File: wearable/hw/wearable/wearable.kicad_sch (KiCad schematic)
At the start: 101 parts, among them J2 Conn_02x05_Odd_Even, J3 USB-C Connector, SW1 SW_Toggle, U1 ADS1299IPAG, U2 TPD1E05U06DYA, U3 BNO080, U4 nPM1300-QEXX, U5 LT3042xMSE, U6 TPS61040DBV, U7 BL54L15-453-000xxx, Y1 32.768kHz, Y2 32.768kHz

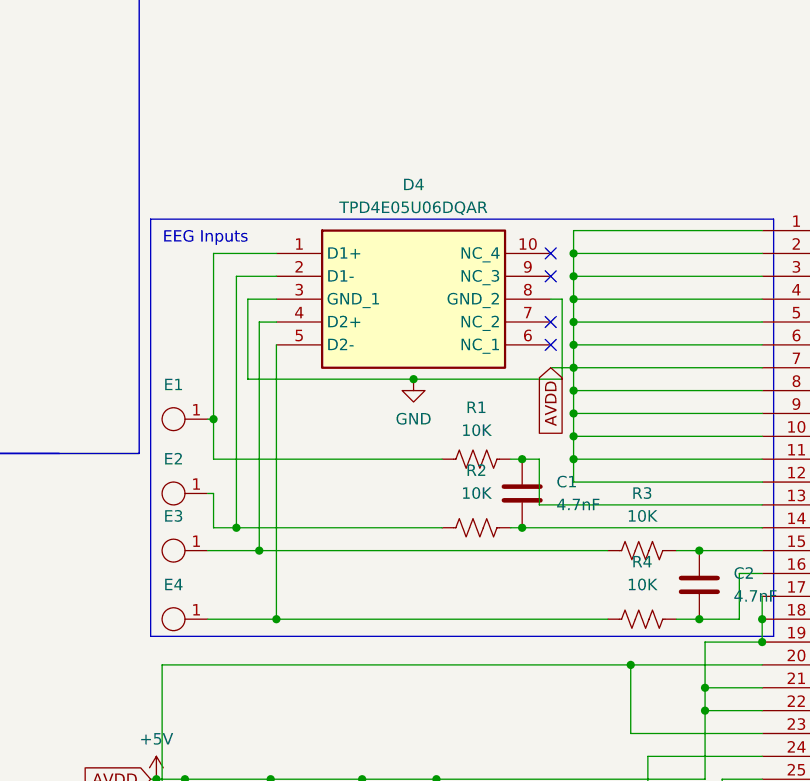
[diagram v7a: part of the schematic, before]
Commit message: Printout documents, reworked analog inputs
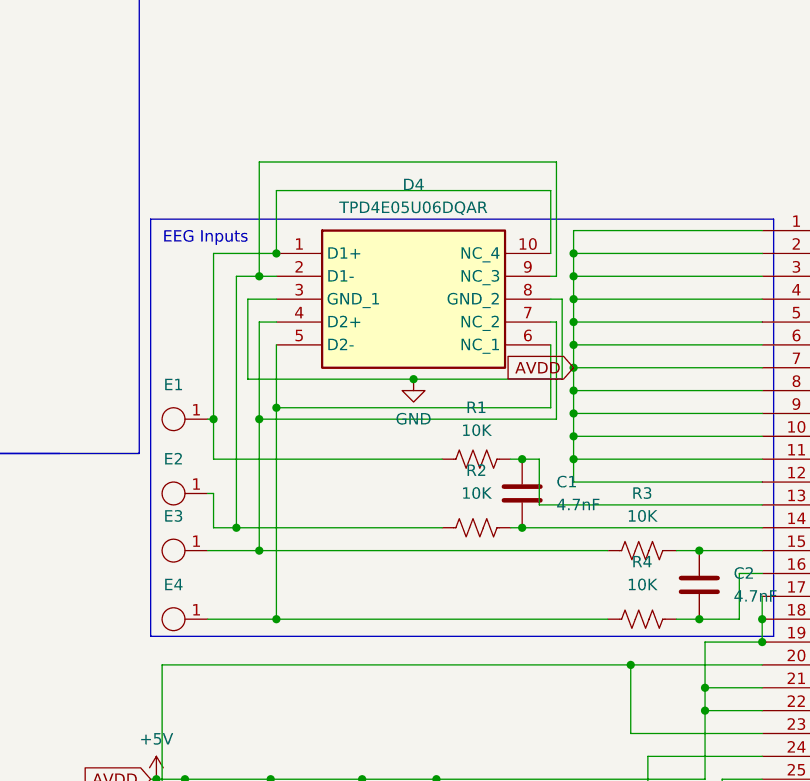
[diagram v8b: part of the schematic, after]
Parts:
- D4: footprint DQA(R-PUSON-N10) -> PCM_Package_SON_AKL:USON-10_2.5x1.0mm_P0.5mm
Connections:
- net at D4.4 (D2+), E3.1, R3.2: now also D4.7 (NC_2)
- net at D4.2 (D1-), E2.1, R2.2: now also D4.9 (NC_3)
- net at D4.1 (D1+), E1.1, R1.2: now also D4.10 (NC_4)
- net at D4.5 (D2-), E4.1, R4.2: now also D4.6 (NC_1)
- no-connect marks 34 -> 30
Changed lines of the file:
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@@
 	)
 	(junction
+		(at 215.265 168.275)
+		(diameter 0)
+		(color 0 0 0 0)
+	)
+	(junction
 		(at 168.275 195.58)
 		(diameter 0)
@@
 	)
 	(junction
+		(at 217.17 182.88)
+		(diameter 0)
+		(color 0 0 0 0)
+	)
+	(junction
 		(at 34.925 288.925)
 		(diameter 0)
@@
 	)
 	(junction
+		(at 217.17 165.735)
+		(diameter 0)
+		(color 0 0 0 0)
+	)
+	(junction
 		(at 10.795 288.925)
 		(diameter 0)
@@
 	)
 	(junction
+		(at 215.265 184.15)
+		(diameter 0)
+		(color 0 0 0 0)
+	)
+	(junction
 		(at 361.315 186.055)
 		(diameter 0)
@@
 	)
 	(no_connect
-		(at 247.65 175.895)
-	)
-	(no_connect
 		(at 299.085 81.915)
 	)
@@
 	)
 	(no_connect
-		(at 247.65 173.355)
-	)
-	(no_connect
 		(at 43.815 235.585)
 	)
@@
 	)
 	(no_connect
-		(at 247.65 168.275)
-	)
-	(no_connect
 		(at 118.745 32.385)
 	)
@@
 	)
 	(no_connect
-		(at 247.65 165.735)
-	)
-	(no_connect
 		(at 118.745 17.145)
 	)
@@
 	(wire
 		(pts
+			(xy 217.17 158.75) (xy 217.17 165.735)
+		)
+		(stroke
+			(width 0)
+			(type default)
+		)
+	)
+	(wire
+		(pts
 			(xy 79.375 203.835) (xy 81.915 203.835)
 		)
@@
 	(wire
 		(pts
-			(xy 217.17 175.895) (xy 217.17 206.375)
+			(xy 217.17 175.895) (xy 217.17 182.88)
 		)
 		(stroke
@@
 	(wire
 		(pts
+			(xy 215.265 168.275) (xy 212.725 168.275)
+		)
+		(stroke
+			(width 0)
+			(type default)
+		)
+	)
+	(wire
+		(pts
 			(xy 19.05 212.725) (xy 19.05 205.105)
 		)
@@
 	(wire
 		(pts
+			(xy 247.65 158.75) (xy 217.17 158.75)
+		)
+		(stroke
+			(width 0)
+			(type default)
+		)
+	)
+	(wire
+		(pts
 			(xy 25.4 282.575) (xy 25.4 288.925)
 		)
@@
 	(wire
 		(pts
-			(xy 247.65 178.435) (xy 250.19 178.435)
-		)
-		(stroke
-			(width 0)
-			(type default)
-		)
-	)
-	(wire
-		(pts
 			(xy 264.795 216.535) (xy 271.145 216.535)
 		)
@@
 	(wire
 		(pts
-			(xy 217.17 168.275) (xy 212.725 168.275)
+			(xy 217.17 168.275) (xy 215.265 168.275)
 		)
 		(stroke
@@
 		)
 	)
+	(wire
+		(pts
+			(xy 215.265 155.575) (xy 215.265 168.275)
+		)
+		(stroke
+			(width 0)
+			(type default)
+		)
+	)
 	(polyline
 		(pts
@@
 	(wire
 		(pts
+			(xy 248.285 173.355) (xy 248.285 184.15)
+		)
+		(stroke
+			(width 0)
+			(type default)
+		)
+	)
+	(wire
+		(pts
 			(xy 266.7 224.155) (xy 266.7 257.81)
 		)
@@
 	(wire
 		(pts
+			(xy 247.65 168.275) (xy 248.285 168.275)
+		)
+		(stroke
+			(width 0)
+			(type default)
+		)
+	)
+	(wire
+		(pts
+			(xy 217.17 182.88) (xy 217.17 206.375)
+		)
+		(stroke
+			(width 0)
+			(type default)
+		)
+	)
+	(wire
+		(pts
 			(xy 118.745 241.935) (xy 114.935 241.935)
 		)
@@
 	(wire
 		(pts
+			(xy 247.65 182.88) (xy 217.17 182.88)
+		)
+		(stroke
+			(width 0)
+			(type default)
+		)
+	)
+	(wire
+		(pts
 			(xy 248.285 71.755) (xy 237.49 71.755)
 		)
@@
 	(wire
 		(pts
+			(xy 215.265 184.15) (xy 215.265 198.755)
+		)
+		(stroke
+			(width 0)
+			(type default)
+		)
+	)
+	(wire
+		(pts
 			(xy 25.4 288.925) (xy 34.925 288.925)
 		)
@@
 	(wire
 		(pts
+			(xy 247.65 173.355) (xy 248.285 173.355)
+		)
+		(stroke
+			(width 0)
+			(type default)
+		)
+	)
+	(wire
+		(pts
 			(xy 250.19 173.355) (xy 250.19 175.895)
 		)
@@
 	(wire
 		(pts
+			(xy 247.65 165.735) (xy 247.65 158.75)
+		)
+		(stroke
+			(width 0)
+			(type default)
+		)
+	)
+	(wire
+		(pts
 			(xy 173.99 258.445) (xy 166.37 258.445)
 		)
@@
 	(wire
 		(pts
+			(xy 247.65 175.895) (xy 247.65 182.88)
+		)
+		(stroke
+			(width 0)
+			(type default)
+		)
+	)
+	(wire
+		(pts
 			(xy 127.635 241.935) (xy 118.745 241.935)
 		)
@@
 	(wire
 		(pts
+			(xy 248.285 155.575) (xy 215.265 155.575)
+		)
+		(stroke
+			(width 0)
+			(type default)
+		)
+	)
+	(wire
+		(pts
 			(xy 158.75 250.825) (xy 166.37 250.825)
 		)
@@
 	(wire
 		(pts
+			(xy 248.285 168.275) (xy 248.285 155.575)
+		)
+		(stroke
+			(width 0)
+			(type default)
+		)
+	)
+	(wire
+		(pts
 			(xy 319.405 71.755) (xy 319.405 71.12)
 		)
@@
 	(wire
 		(pts
-			(xy 215.265 173.355) (xy 215.265 198.755)
+			(xy 248.285 184.15) (xy 215.265 184.15)
+		)
+		(stroke
+			(width 0)
+			(type default)
+		)
+	)
+	(wire
+		(pts
+			(xy 215.265 173.355) (xy 215.265 184.15)
 		)
 		(stroke
@@
 	(global_label "AVDD"
 		(shape input)
-		(at 247.65 178.435 270)
+		(at 250.19 178.435 180)
 		(fields_autoplaced yes)
 		(effects
@@
 		)
 		(property "Intersheetrefs" "${INTERSHEET_REFS}"
-			(at 247.65 186.1374 90)
+			(at 242.4876 178.435 0)
 			(effects
 				(font
@@
 			)
 		)
-		(property "Footprint" "DQA(R-PUSON-N10)"
+		(property "Footprint" "PCM_Package_SON_AKL:USON-10_2.5x1.0mm_P0.5mm"
 			(at 243.84 260.655 0)
 			(effects
